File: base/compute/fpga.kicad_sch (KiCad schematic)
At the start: 12 parts, among them U5 ICE40UP5K-SG48ITR-FPGA_Lattice

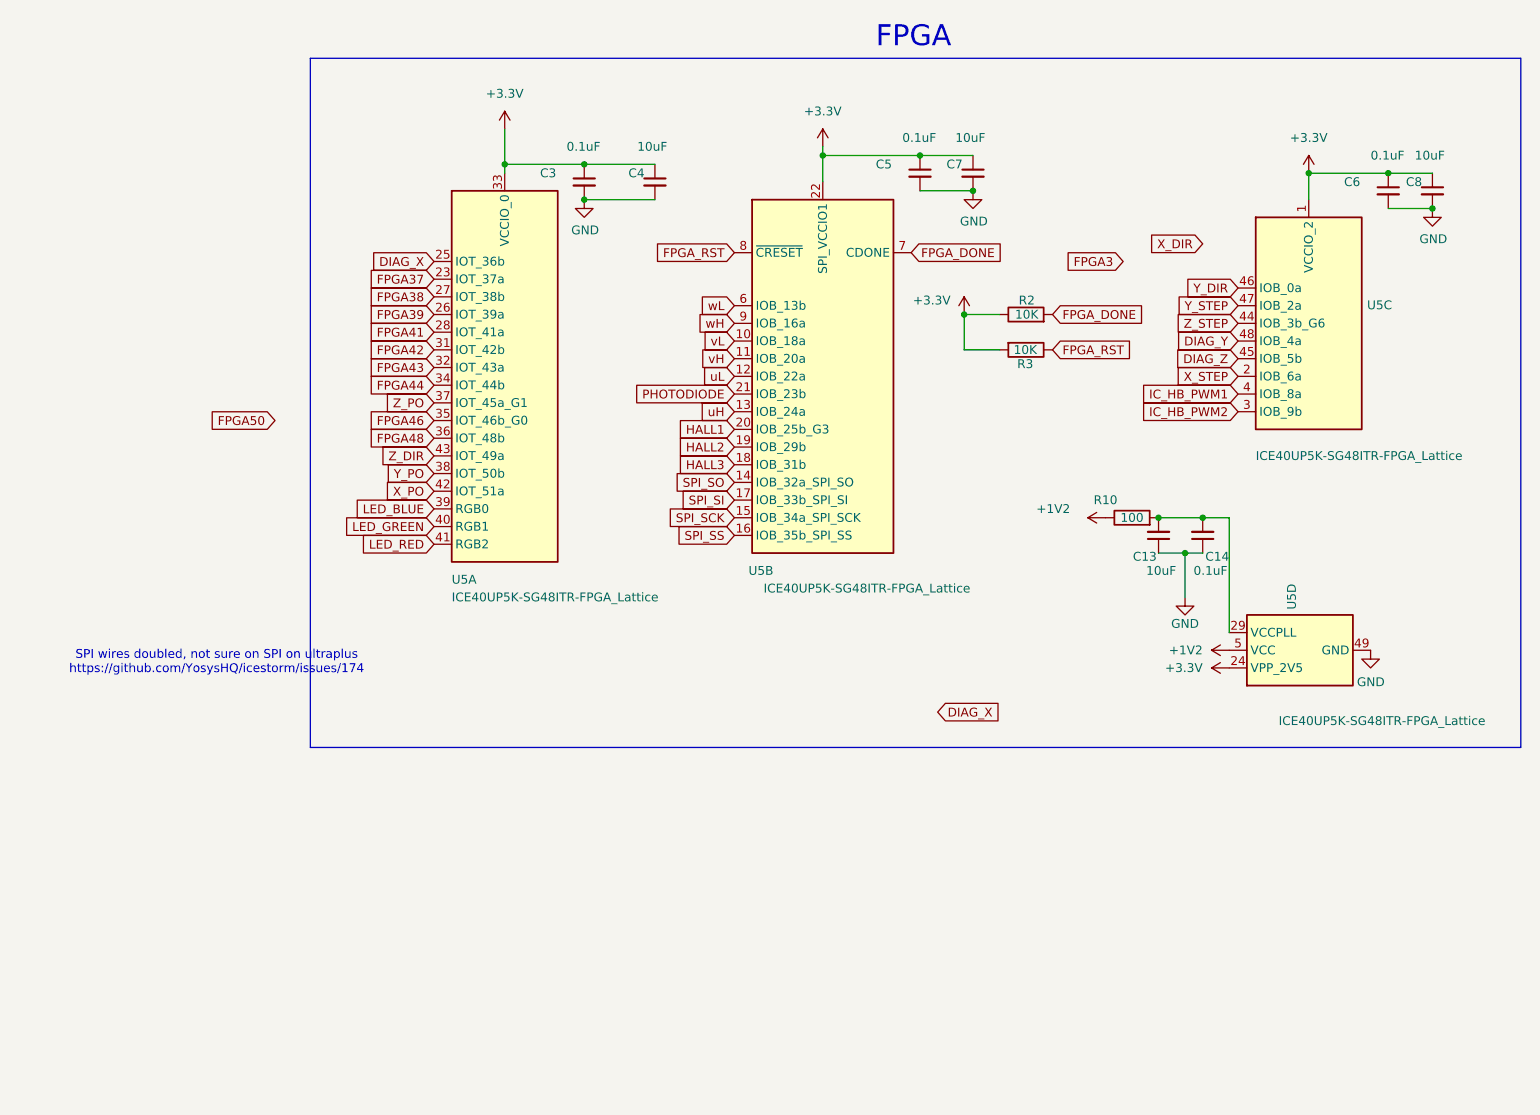
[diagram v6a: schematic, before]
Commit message: schema support spindle, fan , 24V, compliant with VEVOR
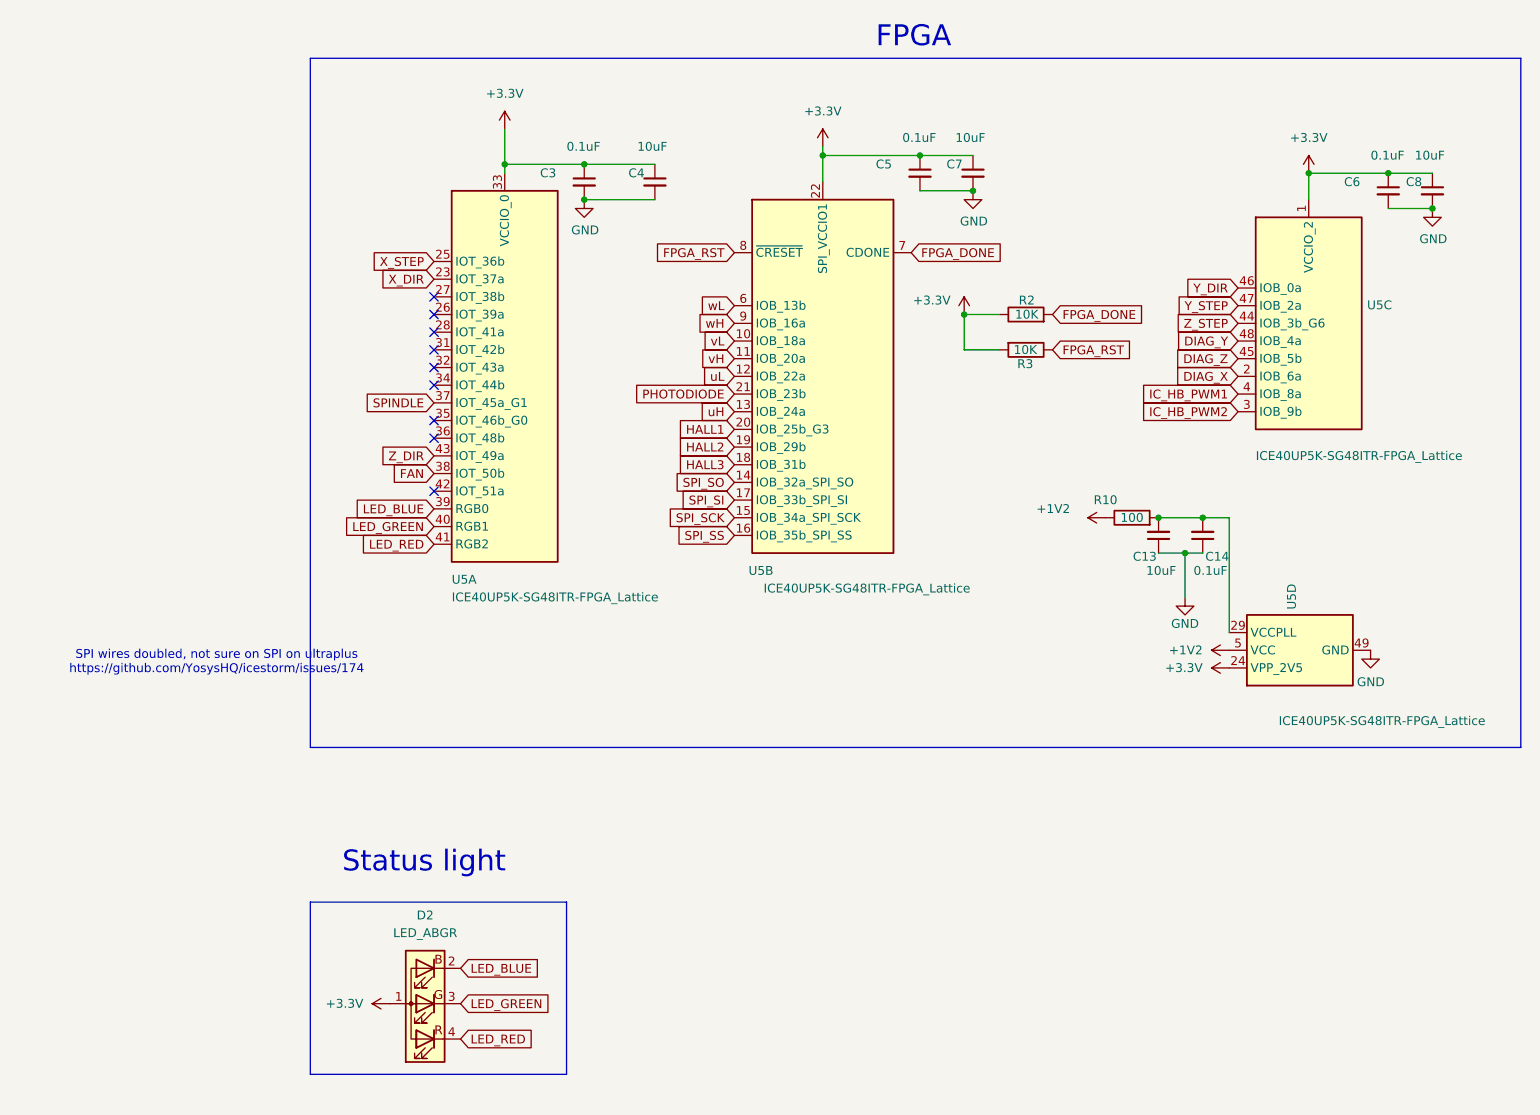
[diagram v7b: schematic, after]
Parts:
- added D2: LED_ABGR, footprints:LED_Cree-PLCC4_2x2mm_CW, symbol Device:LED_ABGR
- C13, C4, C7, C8: farnell# 3010126 -> 3790440; manf# CL21A106KAYNNNE -> GRM21BR61H106KE43L; mouser# 187-CL21A106KAYNNNE -> 81-GRM21BR61H106KE3L
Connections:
- net FPGA37 is gone; now on net X_DIR: U5.23 (IOT_37a)
- net +3.3V: now also D2.1 (A)
- net DIAG_X: now also U5.2 (IOB_6a); no longer U5.25 (IOT_36b)
- net LED_BLUE: now also D2.2 (BK)
- net LED_GREEN: now also D2.3 (GK)
- net LED_RED: now also D2.4 (RK)
- net X_STEP: now also U5.25 (IOT_36b); no longer U5.2 (IOB_6a)
- net FPGA38: no longer names the net of U5.27 (IOT_38b)
- net FPGA39: no longer names the net of U5.26 (IOT_39a)
- net FPGA41: no longer names the net of U5.28 (IOT_41a)
- net FPGA42: no longer names the net of U5.31 (IOT_42b)
- net FPGA43: no longer names the net of U5.32 (IOT_43a)
- net FPGA44: no longer names the net of U5.34 (IOT_44b)
- net FPGA46: no longer names the net of U5.35 (IOT_46b_G0)
- net FPGA48: no longer names the net of U5.36 (IOT_48b)
- net X_PO: no longer names the net of U5.42 (IOT_51a)
- net Y_PO renamed FAN
- net Z_PO renamed SPINDLE
- no-connect marks 0 -> 9
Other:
- note added: "Status light"

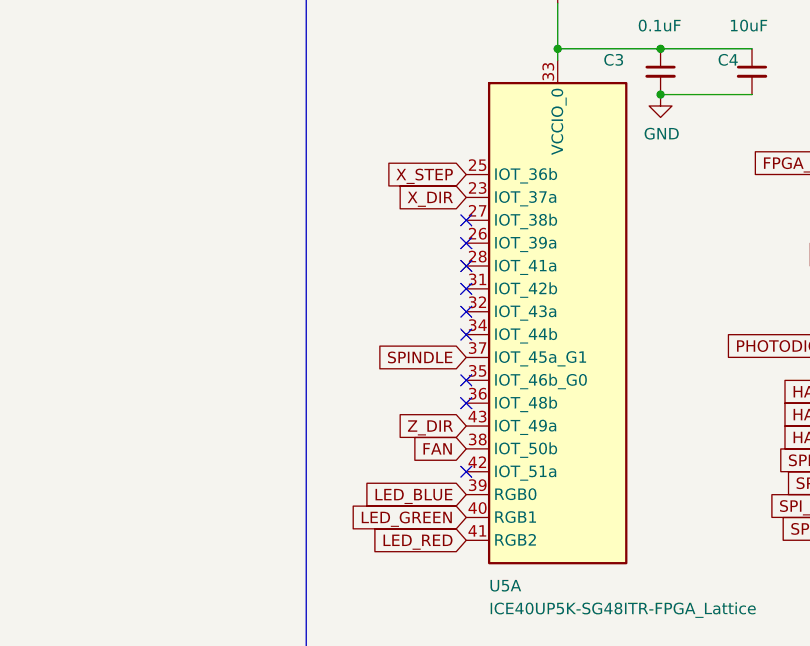
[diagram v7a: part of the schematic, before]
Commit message: board passes all tests
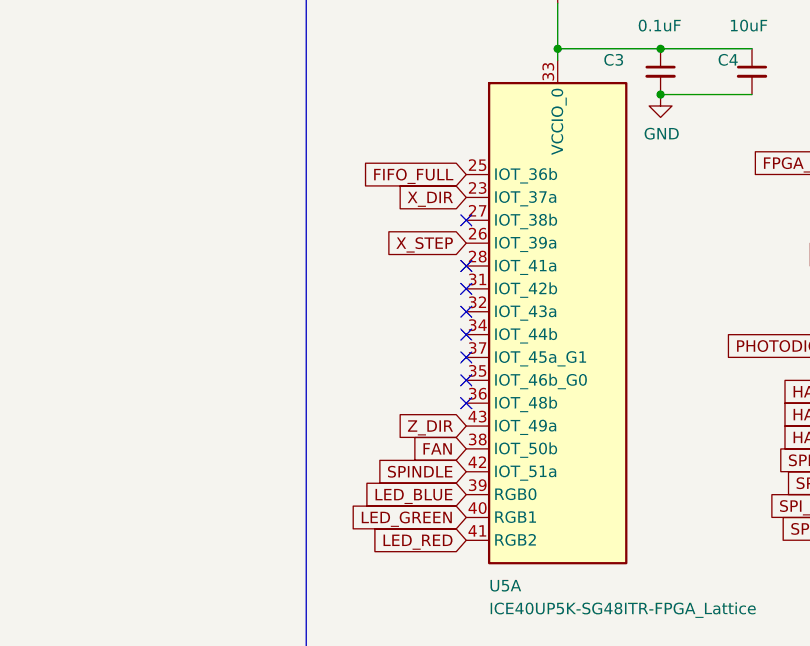
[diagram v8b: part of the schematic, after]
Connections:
- net SPINDLE: now also U5.42 (IOT_51a); no longer U5.37 (IOT_45a_G1)
- net X_STEP: now also U5.26 (IOT_39a); no longer U5.25 (IOT_36b)
- new net FIFO_FULL: U5.25 (IOT_36b)
- no-connect marks 9 -> 8
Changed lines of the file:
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@@
 	(title_block
 		(title "Firestarter ")
-		(date "2024-10-26")
+		(date "2026-04-30")
 		(company "Hexastorm")
 		(comment 1 "v1")
@@
 	)
 	(no_connect
-		(at 73.66 57.15)
+		(at 73.66 59.69)
 	)
 	(no_connect
-		(at 73.66 59.69)
-	)
-	(no_connect
-		(at 73.66 82.55)
+		(at 73.66 69.85)
 	)
 	(no_connect
@@
 		)
 	)
+	(global_label "FIFO_FULL"
+		(shape input)
+		(at 73.66 49.53 180)
+		(fields_autoplaced yes)
+		(effects
+			(font
+				(size 1.27 1.27)
+			)
+			(justify right)
+		)
+		(property "Intersheetrefs" "${INTERSHEET_REFS}"
+			(at 61.7736 49.53 0)
+			(hide yes)
+			(show_name no)
+			(do_not_autoplace no)
+			(effects
+				(font
+					(size 1.27 1.27)
+				)
+				(justify right)
+			)
+		)
+	)
 	(global_label "PHOTODIODE"
 		(shape input)
@@
 	(global_label "X_STEP"
 		(shape input)
-		(at 73.66 49.53 180)
-		(fields_autoplaced yes)
-		(effects
-			(font
-				(size 1.27 1.27)
-			)
-			(justify right)
-		)
-		(property "Intersheetrefs" "${INTERSHEET_REFS}"
-			(at 64.1928 49.53 0)
+		(at 73.66 57.15 180)
+		(fields_autoplaced yes)
+		(effects
+			(font
+				(size 1.27 1.27)
+			)
+			(justify right)
+		)
+		(property "Intersheetrefs" "${INTERSHEET_REFS}"
+			(at 64.1928 57.15 0)
 			(hide yes)
 			(show_name no)
@@
 	(global_label "SPINDLE"
 		(shape input)
-		(at 73.66 69.85 180)
-		(fields_autoplaced yes)
-		(effects
-			(font
-				(size 1.27 1.27)
-			)
-			(justify right)
-		)
-		(property "Intersheetrefs" "${INTERSHEET_REFS}"
-			(at 63.4671 69.85 0)
-			(hide yes)
-			(show_name no)
+		(at 73.66 82.55 180)
+		(fields_autoplaced yes)
+		(effects
+			(font
+				(size 1.27 1.27)
+			)
+			(justify right)
+		)
+		(property "Intersheetrefs" "${INTERSHEET_REFS}"
+			(at 63.4671 82.55 0)
+			(hide yes)
+			(show_name no)
